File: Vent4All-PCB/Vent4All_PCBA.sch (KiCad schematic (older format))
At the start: 0 parts

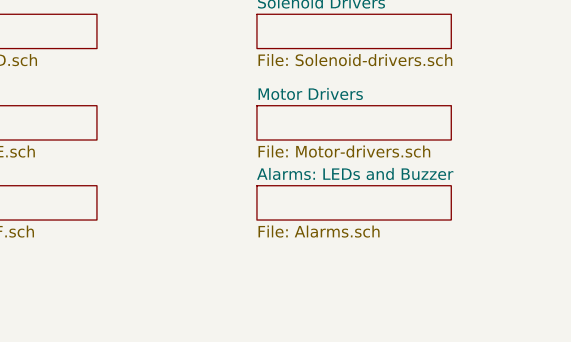
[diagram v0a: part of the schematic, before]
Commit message: Added global labels for reserved communication lines (SPI, I2C, UARTs).
Added hierarchical sheet for external connection interfaces (e.g. to RPi).
Changed symbol libraries table to use ${KIPRJMOD} instead of absolute paths.
When I imported the schematic, KiCAD made a rescue library and changed the line endings of all the .sch files.
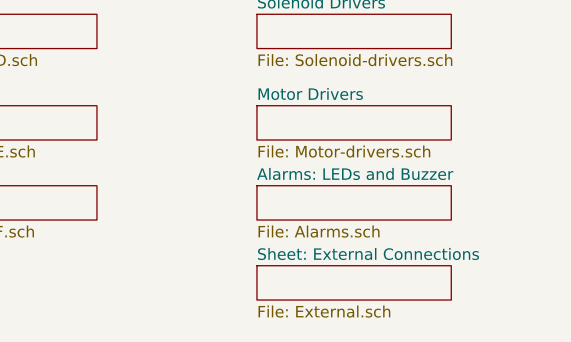
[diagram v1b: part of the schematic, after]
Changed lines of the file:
@@
 F1 "Alarms.sch" 50
 $EndSheet
+$Sheet
+S 3500 3600 850  150
+U 5EB9DB14
+F0 "Sheet: External Connections" 50
+F1 "External.sch" 50
+$EndSheet
 $EndSCHEMATC

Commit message: Added schematic connections for HSC sensors.
Note: this assumes HSC sensors will be soldered directly to the PCB. If we are placing them on daughter boards then we will need to choose the pin header connectors and move the HSC symbols into a separate sheet.
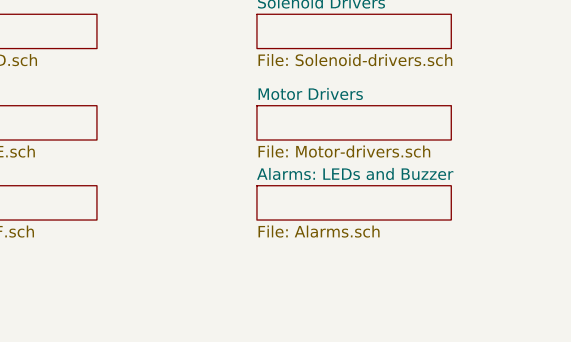
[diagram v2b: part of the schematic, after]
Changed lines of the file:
@@
 F1 "Alarms.sch" 50
 $EndSheet
-$Sheet
-S 3500 3600 850  150
-U 5EB9DB14
-F0 "Sheet: External Connections" 50
-F1 "External.sch" 50
-$EndSheet
 $EndSCHEMATC
